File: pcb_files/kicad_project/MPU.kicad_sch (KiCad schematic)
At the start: 12 parts, among them U2 MPU-6500

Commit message: Actualiza esquemático para añadir SRAM, lectura de corriente y diodo en succión
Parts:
- LSM6DSR1: value ~ -> (none)

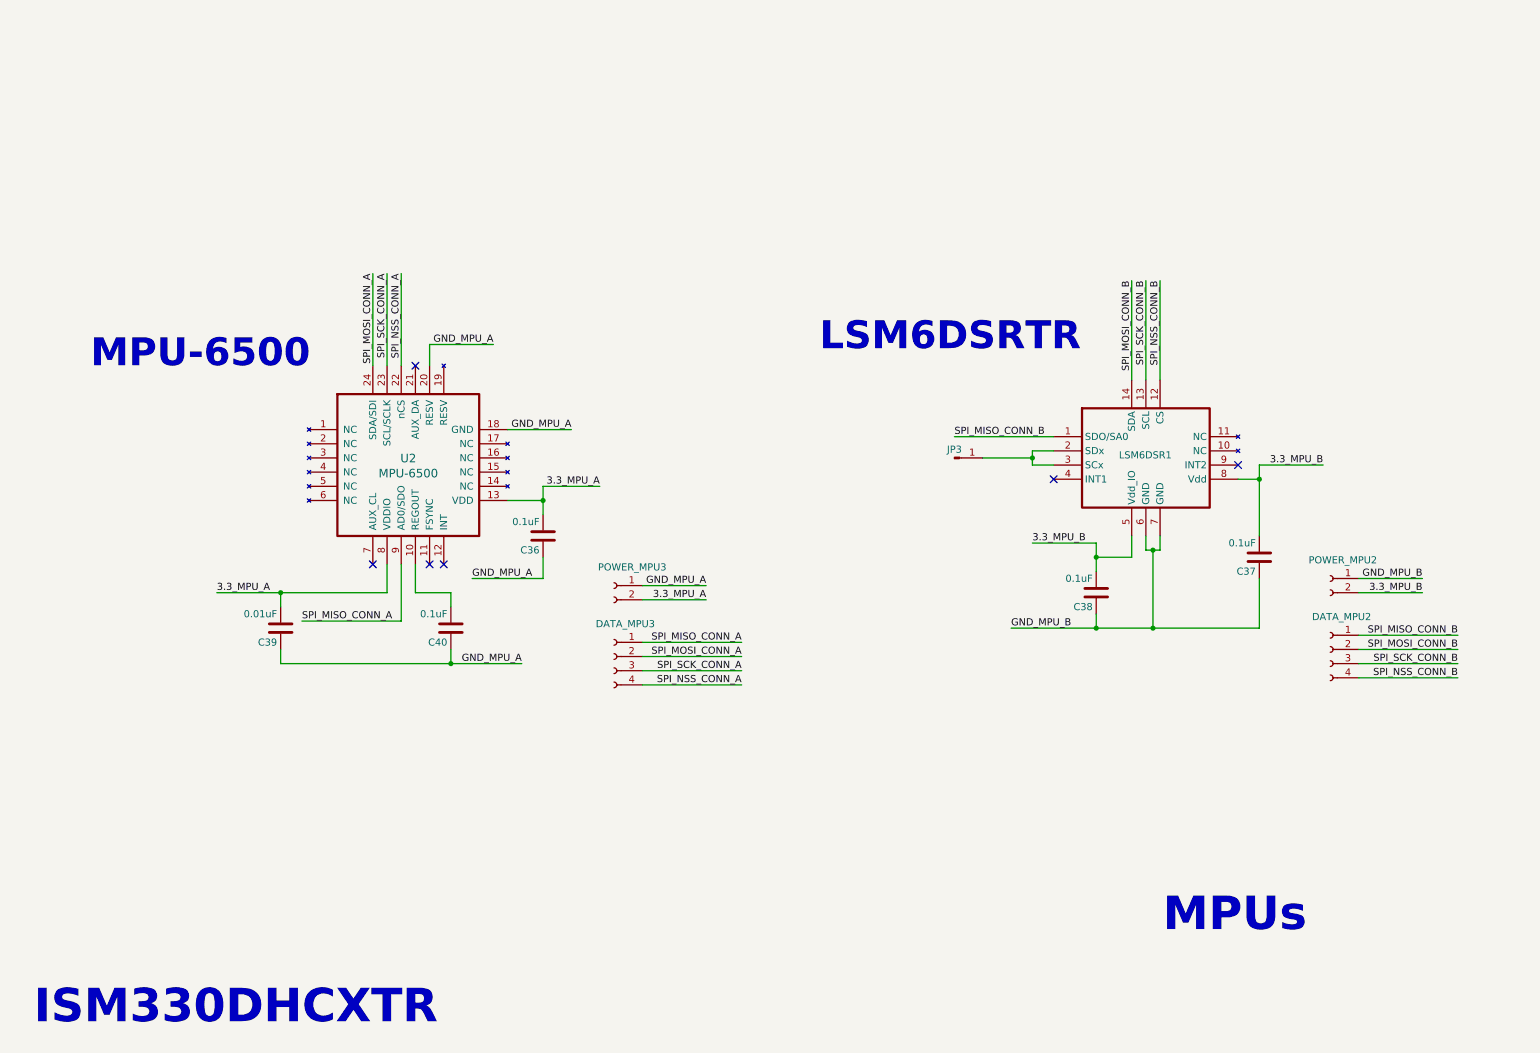
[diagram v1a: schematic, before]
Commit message: Finaliza la version V1.2 con SRAM y correccion de errores.
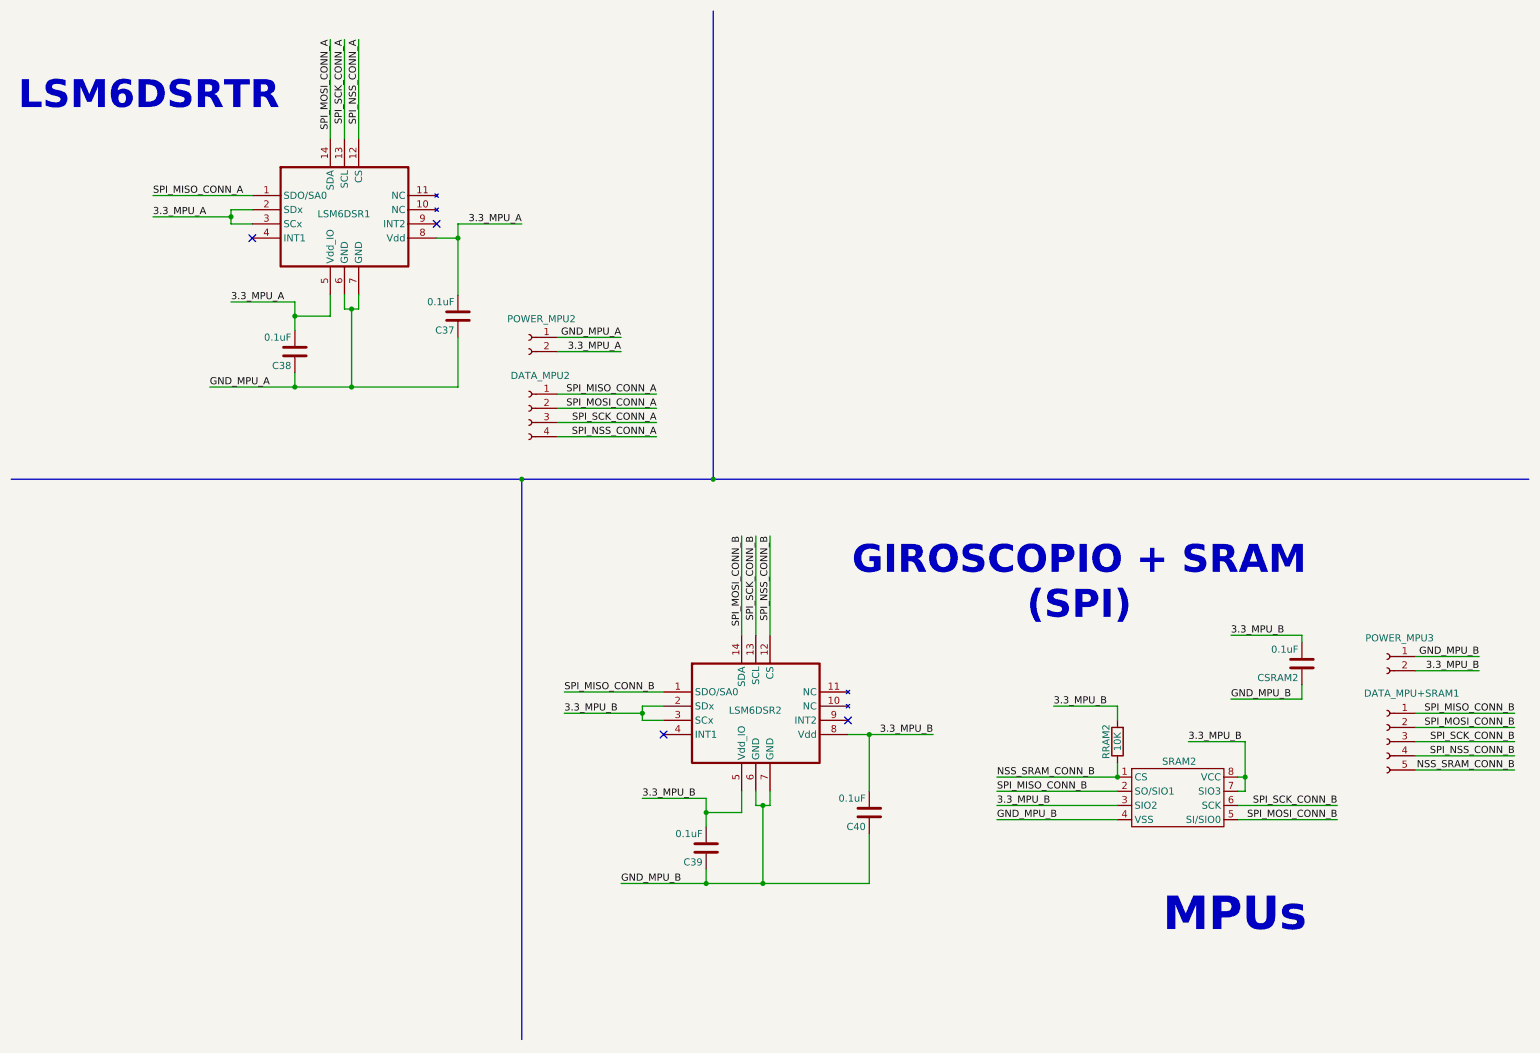
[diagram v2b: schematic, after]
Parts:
- removed C36: 0.1uF, Capacitor_SMD:C_0402_1005Metric_Pad0.74x0.62mm_HandSolder, symbol Device:C
- removed DATA_MPU3: Conn_01x04_Socket, custom_footprints:ZoroBot3_Data_MPU, symbol Connector:Conn_01x04_Socket
- removed JP3: Conn_01x01_Pin, custom_footprints:Generic_simple_1x_SMD_pin, symbol Connector:Conn_01x01_Pin
- removed U2: MPU-6500, Sensor_Motion:InvenSense_QFN-24_3x3mm_P0.4mm, symbol PCB_ZoroBot_v3-rescue:MPU-6500-MPU-6500
- added CSRAM2: 0.1uF, Capacitor_SMD:C_0402_1005Metric_Pad0.74x0.62mm_HandSolder, symbol Device:C
- added DATA_MPU+SRAM1: Conn_01x05_Socket, symbol Connector:Conn_01x05_Socket
- added LSM6DSR2: (no value), Package_LGA:Bosch_LGA-14_3x2.5mm_P0.5mm, symbol custom_symbols:LSM6DSR
- added RRAM2: 10K, Resistor_SMD:R_0402_1005Metric_Pad0.72x0.64mm_HandSolder, symbol Device:R
- added SRAM2: 23AA04M-I/ST, Package_SO:TSSOP-8_4.4x3mm_P0.65mm, symbol custom_symbols:SRAM-23AA04M-I/ST
- C39: value 0.01uF -> 0.1uF
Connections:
- net 3.3_MPU_A: now also C37.2, C38.2, LSM6DSR1.2 (SDx), LSM6DSR1.3 (SCx), LSM6DSR1.5 (Vdd_IO), LSM6DSR1.8 (Vdd), POWER_MPU2.2 (Pin_2); no longer C39.2, POWER_MPU3.2 (Pin_2)
- net 3.3_MPU_B: now also C39.2, C40.2, POWER_MPU3.2 (Pin_2), CSRAM2.2, LSM6DSR2.2 (SDx), LSM6DSR2.3 (SCx), LSM6DSR2.5 (Vdd_IO), LSM6DSR2.8 (Vdd), RRAM2.2, SRAM2.3 (SIO2), SRAM2.7 (SIO3), SRAM2.8 (VCC); no longer C37.2, C38.2, LSM6DSR1.5 (Vdd_IO), LSM6DSR1.8 (Vdd), POWER_MPU2.2 (Pin_2)
- net GND_MPU_A: now also C37.1, C38.1, LSM6DSR1.6 (GND), LSM6DSR1.7 (GND), POWER_MPU2.1 (Pin_1); no longer C39.1, C40.1, POWER_MPU3.1 (Pin_1)
- net GND_MPU_B: now also C39.1, C40.1, POWER_MPU3.1 (Pin_1), CSRAM2.1, LSM6DSR2.6 (GND), LSM6DSR2.7 (GND), SRAM2.4 (VSS); no longer C37.1, C38.1, LSM6DSR1.6 (GND), LSM6DSR1.7 (GND), POWER_MPU2.1 (Pin_1)
- net SPI_MISO_CONN_A: now also DATA_MPU2.1 (Pin_1), LSM6DSR1.1 (SDO/SA0)
- net SPI_MISO_CONN_B: now also DATA_MPU+SRAM1.1 (Pin_1), LSM6DSR2.1 (SDO/SA0), SRAM2.2 (SO/SIO1); no longer DATA_MPU2.1 (Pin_1), LSM6DSR1.1 (SDO/SA0)
- net SPI_MOSI_CONN_A: now also DATA_MPU2.2 (Pin_2), LSM6DSR1.14 (SDA)
- net SPI_MOSI_CONN_B: now also DATA_MPU+SRAM1.2 (Pin_2), LSM6DSR2.14 (SDA), SRAM2.5 (SI/SIO0); no longer DATA_MPU2.2 (Pin_2), LSM6DSR1.14 (SDA)
- net SPI_NSS_CONN_A: now also DATA_MPU2.4 (Pin_4), LSM6DSR1.12 (CS)
- net SPI_NSS_CONN_B: now also DATA_MPU+SRAM1.4 (Pin_4), LSM6DSR2.12 (CS); no longer DATA_MPU2.4 (Pin_4), LSM6DSR1.12 (CS)
- net SPI_SCK_CONN_A: now also DATA_MPU2.3 (Pin_3), LSM6DSR1.13 (SCL)
- net SPI_SCK_CONN_B: now also DATA_MPU+SRAM1.3 (Pin_3), LSM6DSR2.13 (SCL), SRAM2.6 (SCK); no longer DATA_MPU2.3 (Pin_3), LSM6DSR1.13 (SCL)
- new net NSS_SRAM_CONN_B: DATA_MPU+SRAM1.5 (Pin_5), RRAM2.1, SRAM2.1 (CS)
- no-connect marks 6 -> 4
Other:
- note added: "GIROSCOPIO + SRAM (SPI)"
- note removed: "ISM330DHCXTR"
- note removed: "MPU-6500"
- moved on the sheet: C37, C38, DATA_MPU2, LSM6DSR1, POWER_MPU2
